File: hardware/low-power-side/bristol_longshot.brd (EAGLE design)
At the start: 38 x 48.1 mm, 83 parts, among them Q1 NX2301P, U1 SAM_D20E, U10 ADP1607ACPZN-R7, U11 TPS73118DBVT, U12 74LVC1G04GW, U14 SIT1552, U16 SIT1552, U2 SI4461, U3 SE880, U4 SST25WF040BT-40I/NP, U5 TG-5006CJ, U6 TG-5006CJ, U7 ADM6823WYRJZ, U8 SN74LVC1G32DCKR, U9 MS5607-02BA03

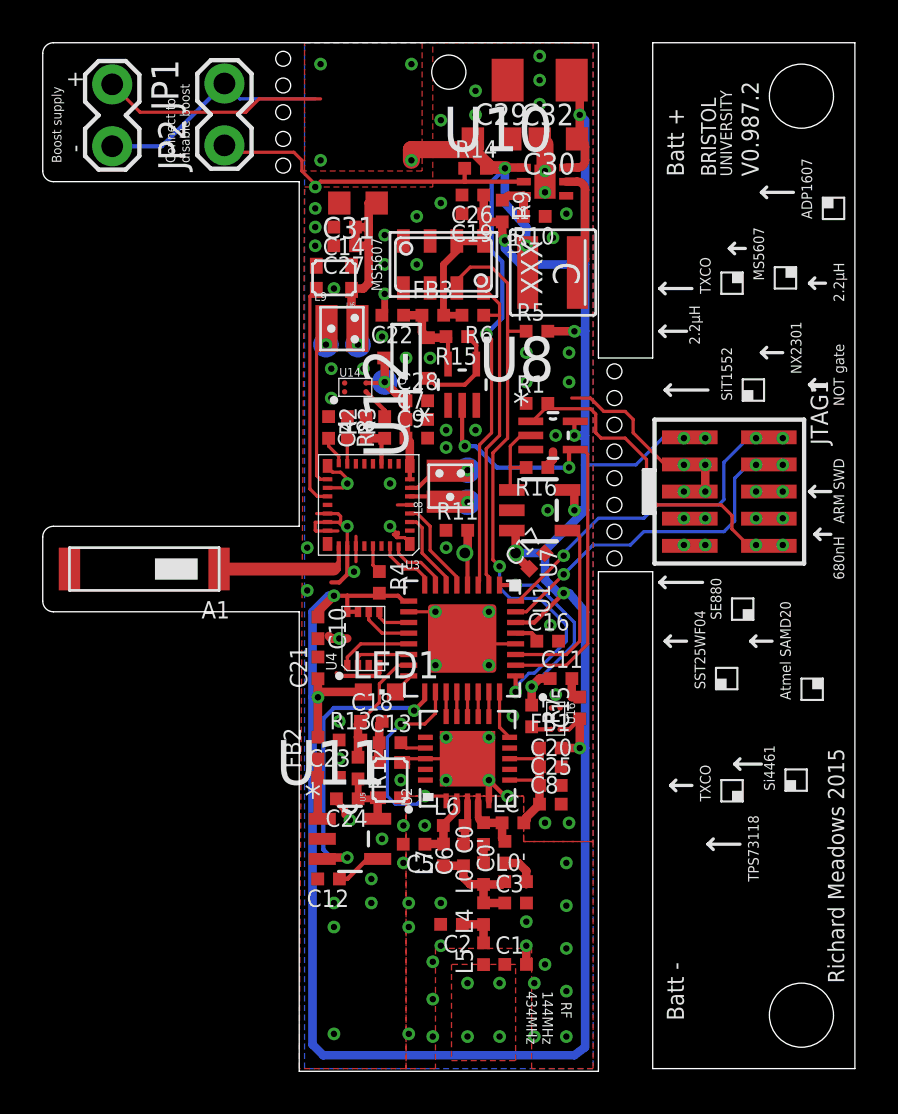
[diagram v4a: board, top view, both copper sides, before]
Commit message: [low-power] v0.987.3 Added pull-down on WDI
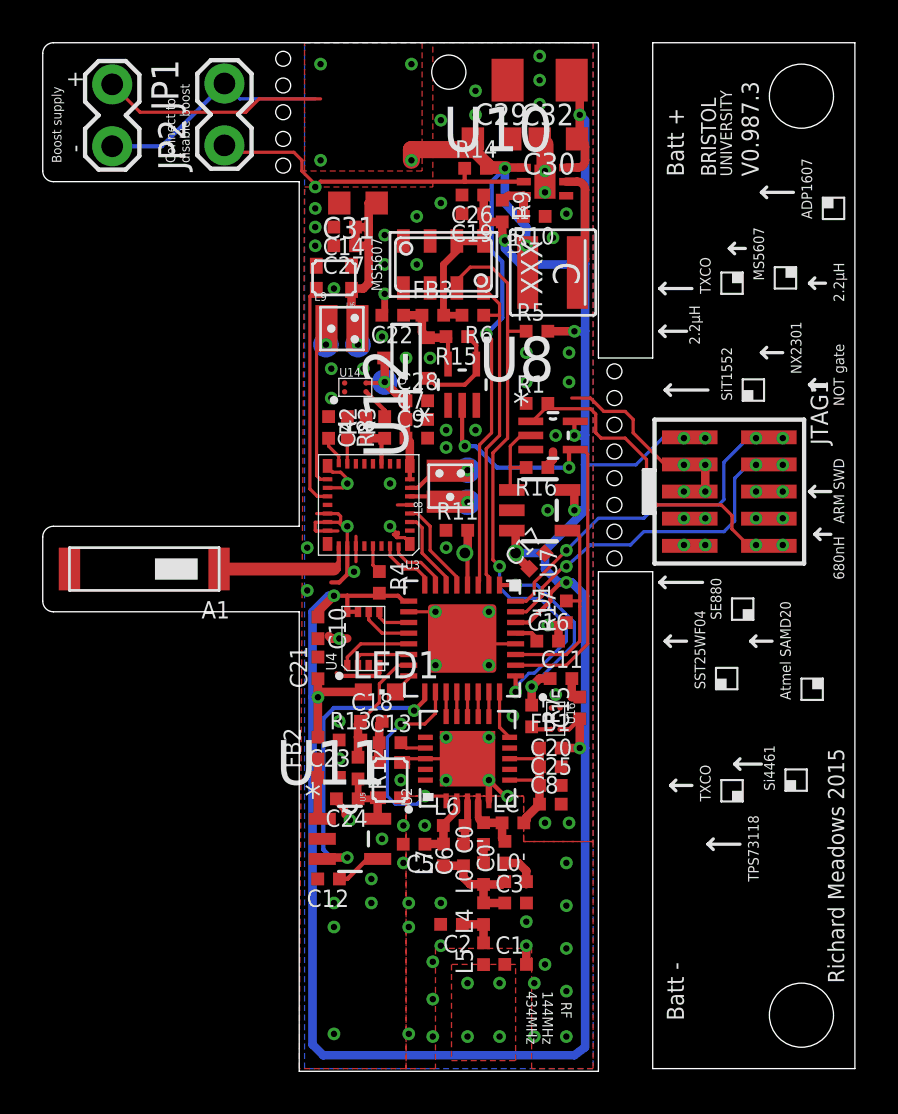
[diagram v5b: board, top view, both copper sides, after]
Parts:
- added R17: 1MΩ, microbuilder_v3:_0402
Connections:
- net GND: now also R17.1
- net WDI: now also R17.2
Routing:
- net GND: track 58.7 -> 60.0 mm
- net 1.8V: track 133.3 -> 133.9 mm
- net WDI: track 8.83 -> 9.46 mm
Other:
- board text added: "V0.987.3"
- board text removed: "V0.987.2"
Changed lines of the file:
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@@
 <circle x="17.125" y="12.125" radius="0.1" width="0.2" layer="21"/>
 <rectangle x1="19.125" y1="0.375" x2="22.125" y2="4.75" layer="29"/>
-<text x="33.5" y="41.75" size="0.8" layer="21" font="vector" ratio="14" rot="R90">V0.987.2</text>
+<text x="33.5" y="41.75" size="0.8" layer="21" font="vector" ratio="14" rot="R90">V0.987.3</text>
 <text x="15.875" y="36.375" size="0.5" layer="21" font="vector" ratio="15" rot="SR90">MS5607</text>
 <text x="35" y="17.25" size="0.5" layer="21" font="vector" ratio="15" rot="SR90">Atmel SAMD20</text>
@@
 <element name="R16" library="microbuilder_v3" package="_0402" value="1MΩ" x="23.125" y="28.125" rot="R180"/>
 <element name="C32" library="resistor" package="C1206K" value="100µF" x="23.25" y="46.25" rot="R180"/>
+<element name="R17" library="microbuilder_v3" package="_0402" value="1MΩ" x="24.5" y="21.375" rot="R90"/>
 </elements>
 <signals>
@@
 <contactref element="R1" pad="1"/>
 <contactref element="R13" pad="1"/>
-<via x="23.75" y="20.75" extent="1-16" drill="0.3"/>
+<via x="23.625" y="20.75" extent="1-16" drill="0.3"/>
 <via x="18.875" y="15.5" extent="1-16" drill="0.3"/>
 <via x="31" y="27" extent="1-16" drill="0.3"/>
@@
 <wire x1="24.75" y1="17.383" x2="25.125" y2="17.383" width="0.4" layer="1"/>
 <contactref element="C32" pad="2"/>
+<contactref element="R17" pad="1"/>
+<wire x1="24.133" y1="20" x2="24.133" y2="20.75" width="0.4" layer="1"/>
+<wire x1="24.133" y1="20.75" x2="23.625" y2="20.75" width="0.4" layer="1"/>
 </signal>
 <signal name="SWDIO">
@@
 <wire x1="33.875" y1="29.625" x2="33.75" y2="29.5" width="0.2" layer="1"/>
 <wire x1="33.75" y1="29.5" x2="33.375" y2="29.5" width="0.2" layer="1"/>
-<via x="24.375" y="24" extent="1-16" drill="0.3"/>
+<via x="24.5" y="24.25" extent="1-16" drill="0.3"/>
 <wire x1="22.125" y1="21.875" x2="22.375" y2="21.875" width="0.1524" layer="1"/>
-<wire x1="24.375" y1="24" x2="24.5" y2="24.25" width="0.1524" layer="16"/>
 <wire x1="24.5" y1="24.25" x2="26" y2="25.75" width="0.1524" layer="16"/>
 <wire x1="26" y1="25.75" x2="28.125" y2="25.75" width="0.1524" layer="16"/>
@@
 <wire x1="31.875" y1="28.375" x2="33" y2="29.5" width="0.1524" layer="16"/>
 <wire x1="33" y1="29.5" x2="33.375" y2="29.5" width="0.1524" layer="16"/>
-<wire x1="24.375" y1="24" x2="22.25" y2="21.875" width="0.1524" layer="1"/>
-<wire x1="22.25" y1="21.875" x2="22.125" y2="21.875" width="0.1524" layer="1"/>
+<wire x1="24.5" y1="24.25" x2="23" y2="22.75" width="0.1524" layer="1"/>
+<wire x1="23" y1="22.75" x2="23" y2="22.25" width="0.1524" layer="1"/>
+<wire x1="23" y1="22.25" x2="22.625" y2="21.875" width="0.1524" layer="1"/>
+<wire x1="22.625" y1="21.875" x2="22.125" y2="21.875" width="0.1524" layer="1"/>
 </signal>
 <signal name="SWDCLK">
@@
 <wire x1="34.625" y1="28.25" x2="34.605" y2="28.27" width="0.2" layer="1"/>
 <wire x1="34.605" y1="28.27" x2="33.975" y2="28.27" width="0.2" layer="1"/>
-<via x="24.375" y="23.125" extent="1-16" drill="0.3"/>
-<wire x1="22.625" y1="21.375" x2="24.375" y2="23.125" width="0.1524" layer="1"/>
-<wire x1="24.375" y1="23.125" x2="25.75" y2="24.5" width="0.1524" layer="16"/>
-<wire x1="25.75" y1="24.5" x2="27.5" y2="24.5" width="0.1524" layer="16"/>
+<via x="24.5" y="23.5" extent="1-16" drill="0.3"/>
+<wire x1="22.625" y1="21.375" x2="23.375" y2="22.125" width="0.1524" layer="1"/>
+<wire x1="23.375" y1="22.125" x2="23.375" y2="22.5" width="0.1524" layer="1"/>
+<wire x1="23.375" y1="22.5" x2="24.375" y2="23.5" width="0.1524" layer="1"/>
+<wire x1="24.375" y1="23.5" x2="24.5" y2="23.5" width="0.1524" layer="1"/>
+<wire x1="24.5" y1="23.5" x2="25.625" y2="24.5" width="0.1524" layer="16"/>
+<wire x1="25.625" y1="24.5" x2="27.5" y2="24.5" width="0.1524" layer="16"/>
 <wire x1="27.5" y1="24.5" x2="28.125" y2="25.125" width="0.1524" layer="16"/>
 <wire x1="28.125" y1="25.125" x2="31.875" y2="25.125" width="0.1524" layer="16"/>
@@
 <wire x1="22.125" y1="19.375" x2="24.5" y2="19.375" width="0.1524" layer="1"/>
 <wire x1="24.5" y1="19.375" x2="25.125" y2="20" width="0.1524" layer="1"/>
-<wire x1="25.125" y1="20" x2="25.125" y2="24.875" width="0.1524" layer="1"/>
+<wire x1="25.125" y1="20" x2="25.125" y2="21.625" width="0.1524" layer="1"/>
+<wire x1="25.125" y1="21.883" x2="25.125" y2="24.875" width="0.1524" layer="1"/>
 <wire x1="25.125" y1="24.875" x2="24.825" y2="25.175" width="0.1524" layer="1"/>
 <wire x1="24.825" y1="25.175" x2="24.5501" y2="25.175" width="0.1524" layer="1"/>
+<contactref element="R17" pad="2"/>
+<wire x1="24.5" y1="21.883" x2="25.125" y2="21.883" width="0.1524" layer="1"/>
+<wire x1="25.125" y1="21.883" x2="25.125" y2="21.625" width="0.1524" layer="1"/>
 </signal>
 <signal name="RADIO_XIN">
@@
 <contactref element="LED1" pad="A"/>
 <via x="12.875" y="17.375" extent="1-16" drill="0.3"/>
-<via x="24.375" y="22.25" extent="1-16" drill="0.3"/>
-<wire x1="22.125" y1="20.875" x2="23" y2="20.875" width="0.2" layer="1"/>
-<wire x1="24.375" y1="22.25" x2="24.625" y2="22.25" width="0.4" layer="16"/>
-<wire x1="24.625" y1="22.25" x2="25.375" y2="21.375" width="0.4" layer="16"/>
+<via x="24.5" y="22.75" extent="1-16" drill="0.3"/>
+<wire x1="22.125" y1="20.875" x2="22.75" y2="20.875" width="0.2" layer="1"/>
+<wire x1="24.5" y1="22.75" x2="24.75" y2="22.75" width="0.4" layer="16"/>
+<wire x1="24.75" y1="22.75" x2="25.375" y2="22.125" width="0.4" layer="16"/>
 <via x="25.125" y="15" extent="1-16" drill="0.3"/>
 <contactref element="C17" pad="1"/>
@@
 <wire x1="12.625" y1="21.375" x2="12.625" y2="17.375" width="0.4" layer="16"/>
 <wire x1="12.625" y1="17.375" x2="12.875" y2="17.375" width="0.4" layer="16"/>
-<wire x1="23" y1="20.875" x2="24.375" y2="22.25" width="0.2" layer="1"/>
+<wire x1="22.75" y1="20.875" x2="23.75" y2="21.875" width="0.2" layer="1"/>
+<wire x1="23.75" y1="21.875" x2="23.75" y2="22.25" width="0.2" layer="1"/>
+<wire x1="23.75" y1="22.25" x2="24.25" y2="22.75" width="0.2" layer="1"/>
+<wire x1="24.25" y1="22.75" x2="24.5" y2="22.75" width="0.2" layer="1"/>
 <contactref element="U9" pad="2"/>
 <contactref element="C19" pad="1"/>
@@
 <wire x1="24.875" y1="0.625" x2="25.375" y2="1" width="0.4" layer="16"/>
 <wire x1="25.375" y1="1" x2="25.375" y2="15" width="0.4" layer="16"/>
-<wire x1="25.375" y1="15" x2="25.375" y2="21.375" width="0.4" layer="16"/>
+<wire x1="25.375" y1="15" x2="25.375" y2="22.125" width="0.4" layer="16"/>
 <wire x1="25.125" y1="44.625" x2="25.125" y2="46" width="0.4" layer="1"/>
 <wire x1="25.375" y1="28.25" x2="27.75" y2="28.25" width="0.1524" layer="16"/>
@@
 <wire x1="25.375" y1="26.125" x2="23.5" y2="24.25" width="0.4" layer="16"/>
 <wire x1="23.5" y1="24.25" x2="23.5" y2="24.125" width="0.4" layer="16"/>
-<wire x1="23.5" y1="24.125" x2="23.5" y2="22.875" width="0.4" layer="16"/>
-<wire x1="23.5" y1="22.875" x2="24.125" y2="22.25" width="0.4" layer="16"/>
-<wire x1="24.125" y1="22.25" x2="24.375" y2="22.25" width="0.4" layer="16"/>
+<wire x1="23.5" y1="24.125" x2="23.5" y2="23.375" width="0.4" layer="16"/>
+<wire x1="23.5" y1="23.375" x2="24.125" y2="22.75" width="0.4" layer="16"/>
+<wire x1="24.125" y1="22.75" x2="24.5" y2="22.75" width="0.4" layer="16"/>
 <wire x1="22.125" y1="24.125" x2="23.5" y2="24.125" width="0.4" layer="16"/>
 <wire x1="21.9999" y1="25.125" x2="22.125" y2="25.1251" width="0.4" layer="1"/>
